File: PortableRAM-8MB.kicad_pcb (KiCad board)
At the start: 4 copper layers, 123 x 81 mm, 37 parts, among them J1 RAM Connector, J2 JTAG_Header_2.54mm_1x06, U1 ATF1502ASL, U11 74HC245, U12 74HC245, U2 AS6C8008-55TIN, U3 AS6C8008-55TIN, U4 AS6C8008-55TIN, U5 AS6C8008-55TIN, U6 AS6C8008-55TIN, U7 AS6C8008-55TIN, U8 AS6C8008-55TIN, U9 AS6C8008-55TIN

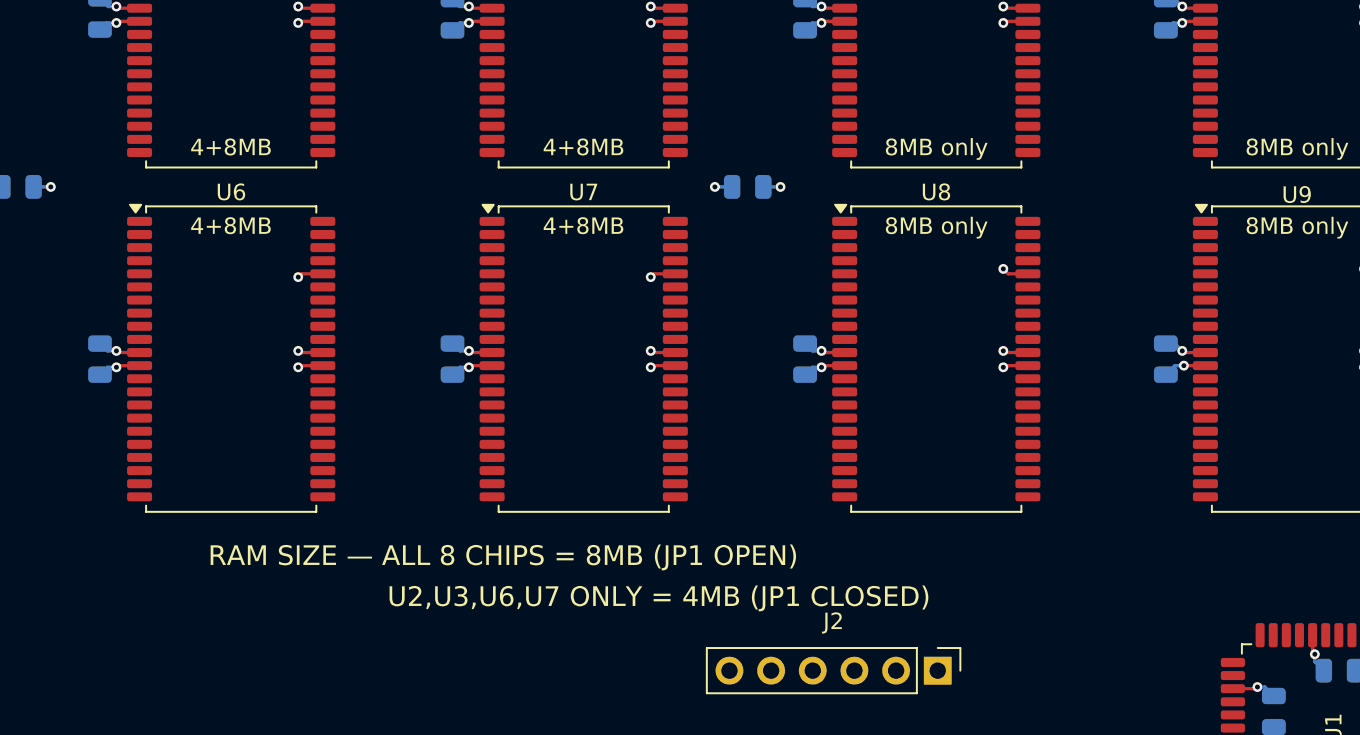
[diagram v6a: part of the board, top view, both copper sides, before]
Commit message: PCB: BANKSEL hand-routed; footprints locked
BANKSEL (CPLD pin 33 -> A19 on all 8 SRAMs) routed as a 4-spine
fishbone on F.Cu; verified all 8 chips on one net. All 37 footprints
locked. Track/via locking still pending (Ctrl+A caught footprints
only — Selection Filter excluded tracks).

Co-Authored-By: Claude Fable 5 <noreply@anthropic.com>
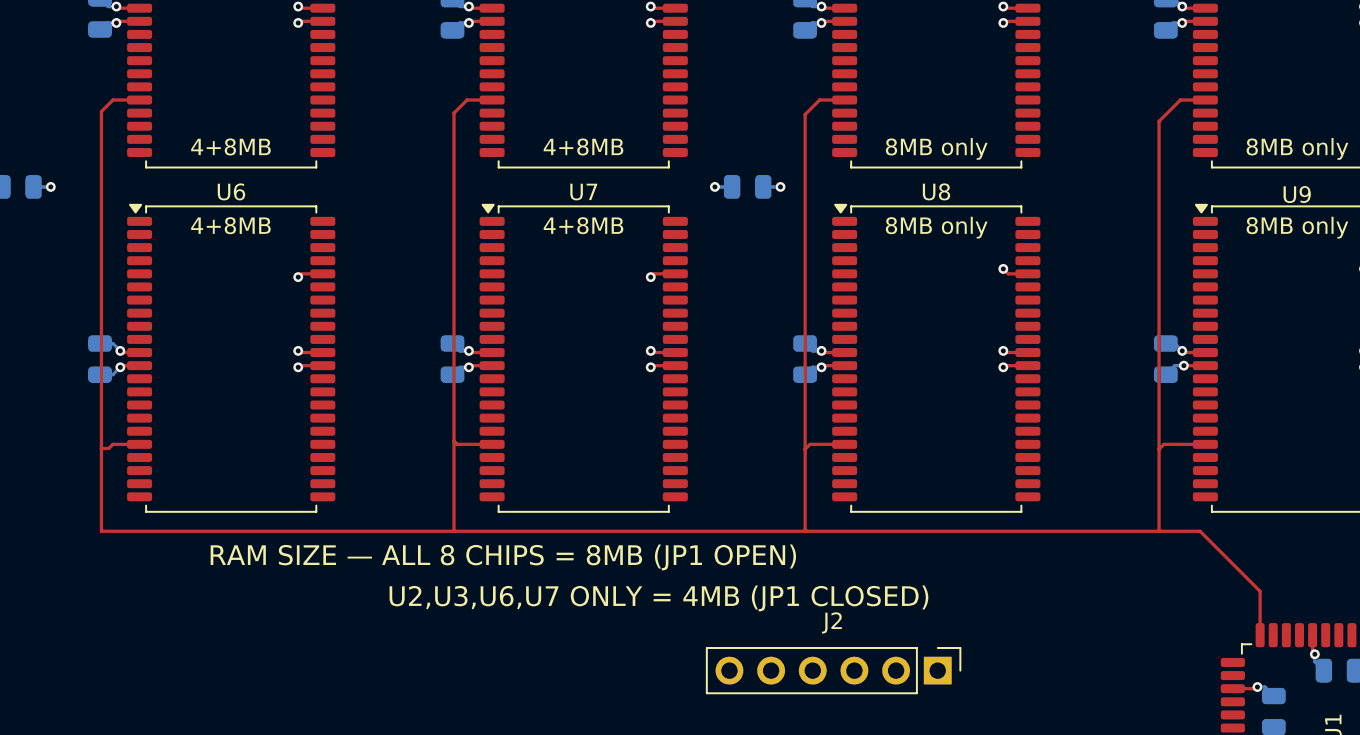
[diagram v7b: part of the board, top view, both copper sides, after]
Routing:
- net /BANKSEL: track 0.00 -> 198.2 mm
